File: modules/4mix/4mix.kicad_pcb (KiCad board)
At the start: 4 copper layers, 91.4 x 68.6 mm, 167 parts, among them U1 MCP6002-xSN, U10 MCP6002-xSN, U11 MCP6002-xSN, U2 MCP6002-xSN, U3 MCP6002-xSN, U4 MCP6002-xSN, U5 MCP6002-xSN, U6 MCP6002-xSN, U7 MCP6002-xSN, U8 MCP6002-xSN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

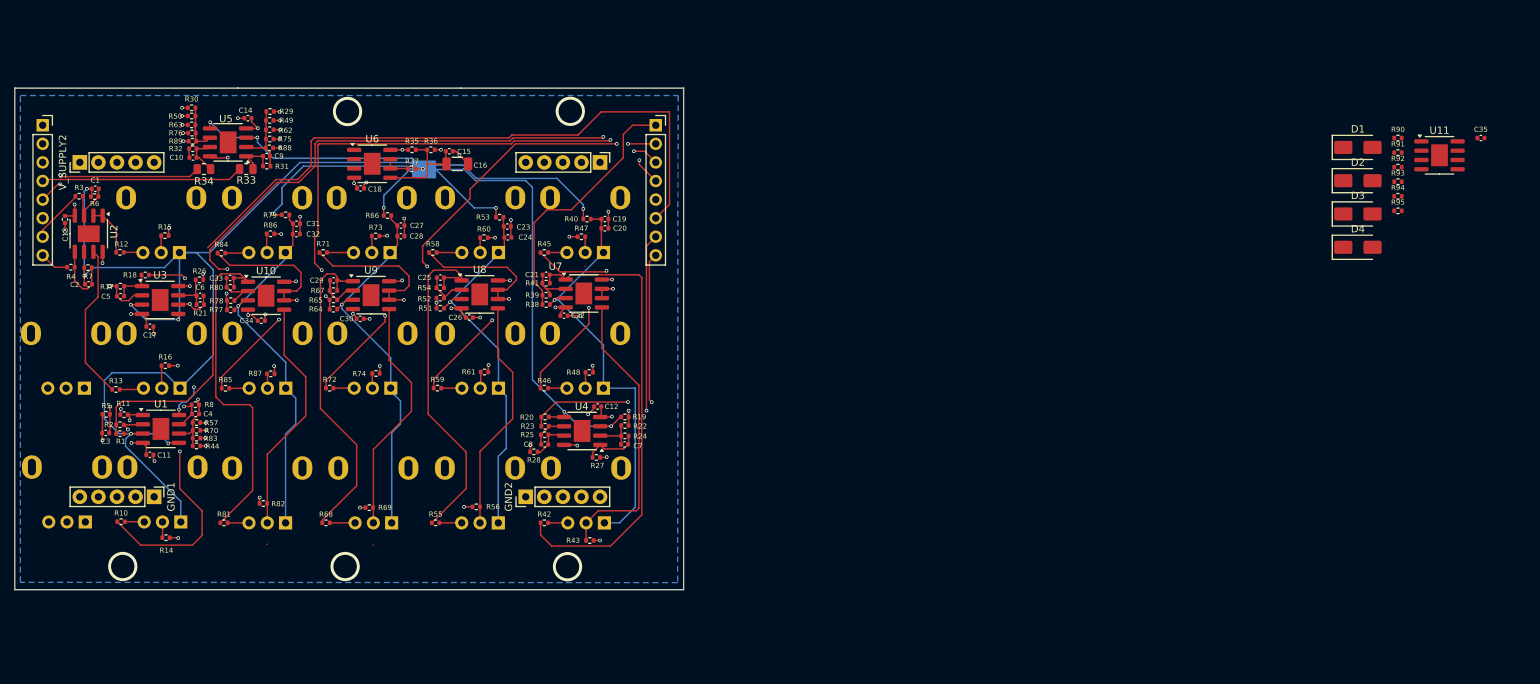
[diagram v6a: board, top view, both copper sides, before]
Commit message: Finialize all the routing
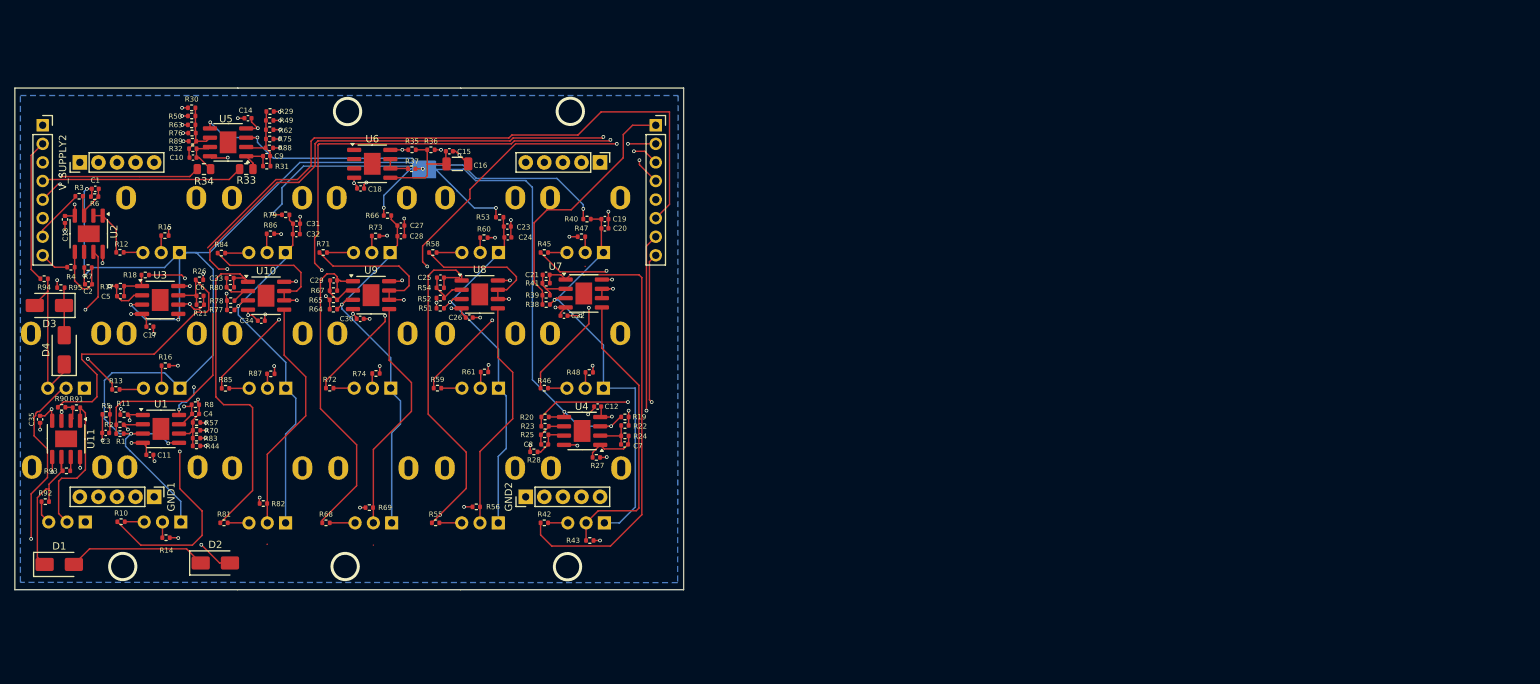
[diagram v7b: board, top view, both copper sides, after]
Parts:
- moved C35 200.7 mm to (50.4, 85.9), turned to 90 degrees
- moved U11 191.7 mm to (54.0, 88.6), turned to -90 degrees
- moved R92 190.5 mm to (51.2, 97.2)
- moved D1 186.5 mm to (53.1, 105.8)
- moved R90 186.4 mm to (53.4, 84.3)
- moved R93 186.3 mm to (54.0, 93.0)
- moved R94 185.4 mm to (51.0, 66.7), turned to 180 degrees
- moved R91 184.0 mm to (55.4, 84.3)
- moved R95 183.1 mm to (53.3, 67.9), turned to 180 degrees
- moved D3 179.3 mm to (51.7, 70.4), turned to 180 degrees
- moved D4 177.4 mm to (53.7, 76.4), turned to 90 degrees
- moved D2 164.7 mm to (74.4, 105.6)
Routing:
- net Net-(D2-A): track 0.00 -> 53.0 mm, vias 0 -> 2
- net /Overdrive/INPUT: track 5.97 -> 43.3 mm
- net Net-(D3-A): track 0.00 -> 23.7 mm
- net OD_DIRTY: track 0.00 -> 21.1 mm, vias 0 -> 1
- net Net-(R91-Pad2): track 0.00 -> 20.9 mm
- net Net-(D1-K): track 0.00 -> 20.4 mm
- net OD_CLEAN: track 0.00 -> 19.6 mm
- net Net-(D1-A): track 0.00 -> 19.0 mm
- net Net-(D3-K): track 0.00 -> 6.55 mm
- net GND: track 41.0 -> 44.6 mm, vias 16 -> 17
- net V_MID: track 331.6 -> 334.9 mm, vias 16 -> 18
- net Net-(R92-Pad1): track 0.00 -> 3.18 mm
- net Net-(U11A--): track 0.00 -> 2.94 mm
- net V_SUPPLY: track 32.4 -> 34.9 mm, vias 21 -> 23
- net Net-(U2B--): track 21.3 -> 22.1 mm, vias 0 -> 2

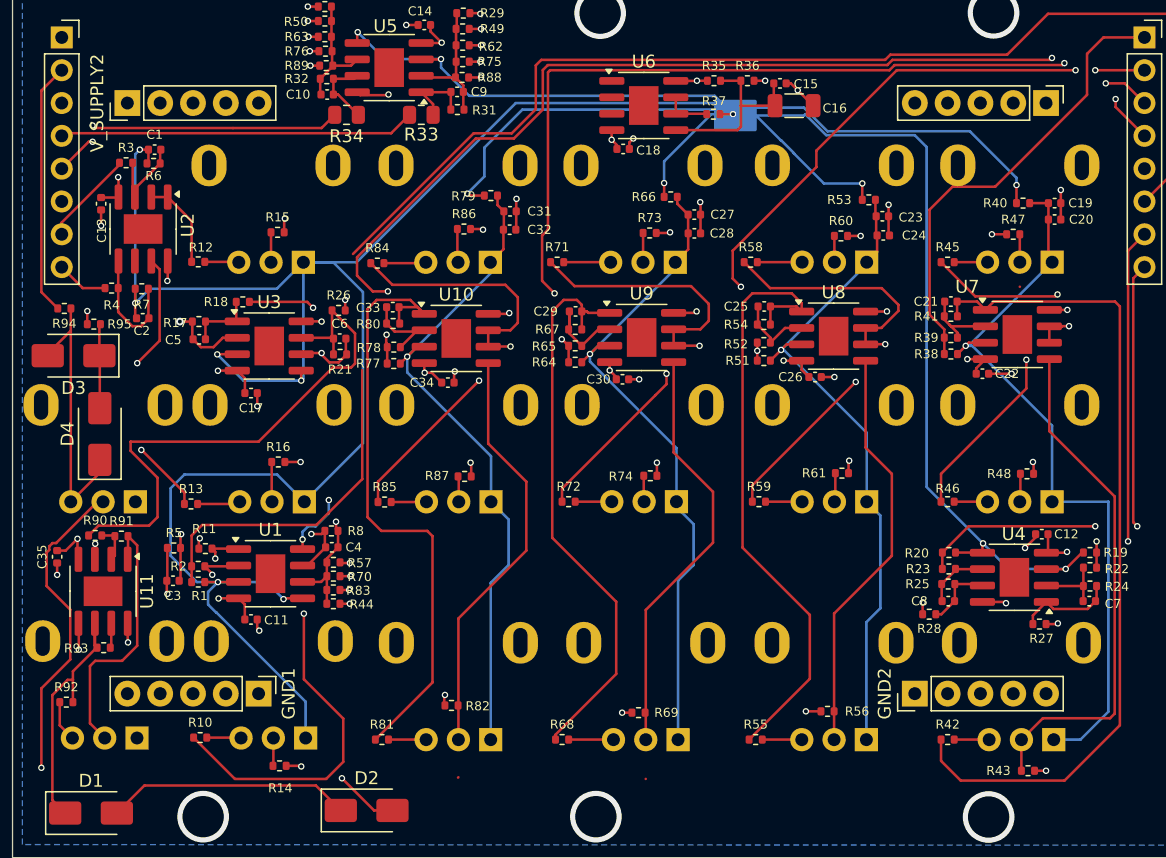
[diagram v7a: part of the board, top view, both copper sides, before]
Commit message: Fix all the routing issues
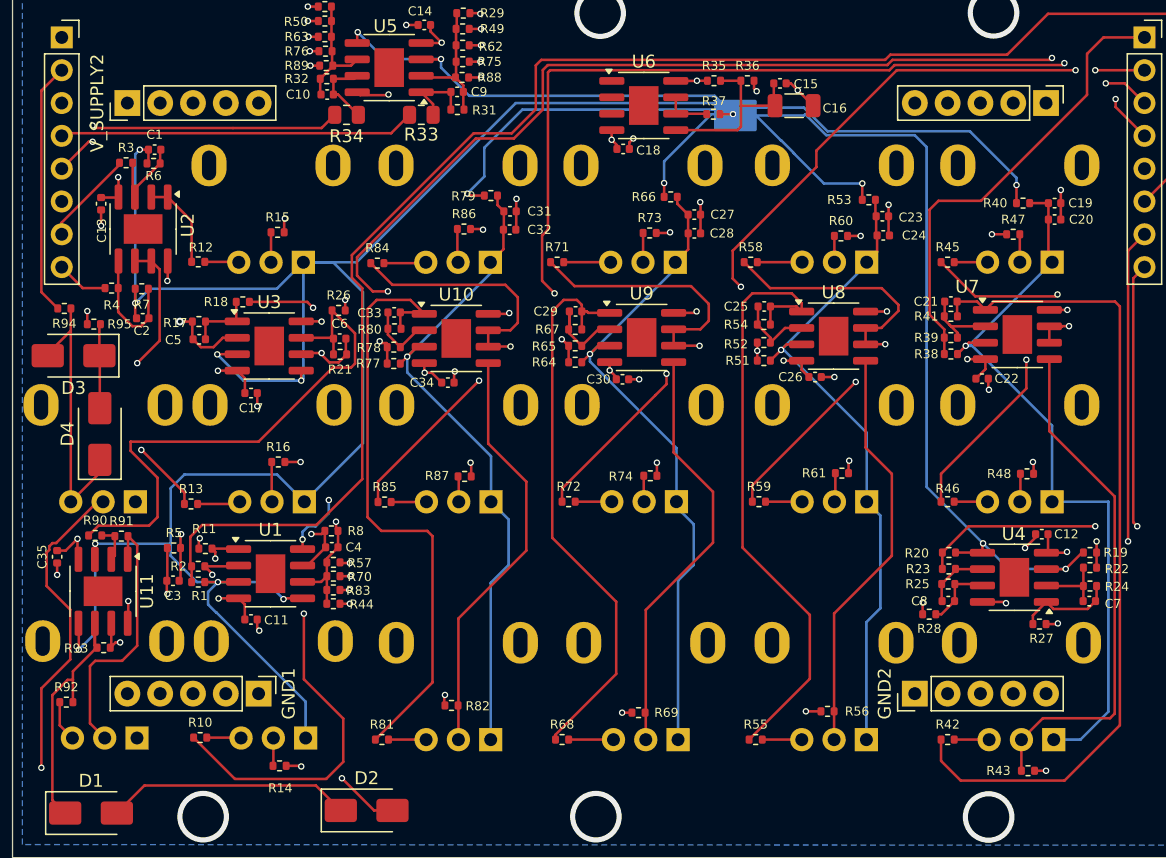
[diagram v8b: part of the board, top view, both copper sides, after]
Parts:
- moved R80 0.42 mm to (76.6, 68.3)
- moved C33 0.42 mm to (76.5, 67.0)
- moved C22 0.38 mm to (122.0, 72.1)
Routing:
- net V_MID: track 334.9 -> 349.4 mm, vias 18 -> 17
- net Net-(D3-A): track 23.7 -> 37.8 mm, vias 0 -> 1
- net IN_MIXOUT: track 115.2 -> 124.7 mm
- net Net-(U10A--): track 6.88 -> 5.49 mm
- net Net-(U2B--): track 22.1 -> 23.3 mm
- net V_SUPPLY: track 34.9 -> 34.2 mm
- net IN_4: track 83.3 -> 84.0 mm
- net (no net): vias 4 -> 5
